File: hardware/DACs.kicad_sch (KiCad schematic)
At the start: 72 parts, among them J20 Conn_01x02, J21 Conn_01x02, U10 LT1678CS8#PBF, U11 LT1678CS8#PBF, U12 LT1678CS8#PBF, U13 LT1678CS8#PBF, U14 LT1461CIS8-2.5#PBF, U6 LTC2642ACDD-16#PBF, U7 LTC2642ACDD-16#PBF, U8 LTC2642ACDD-16#PBF, U9 LTC2642ACDD-16#PBF

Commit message: Some improvements have been made to the layout.
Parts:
- renumbered RShunt1 to RSh1, RShunt2 to RSh2, RShunt3 to RSh3, RShunt4 to RSh4
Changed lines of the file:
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@@
 		(on_board yes)
 		(dnp no)
-		(property "Reference" "RShunt4"
+		(property "Reference" "RSh4"
 			(at 181.102 141.224 0)
 			(effects
@@
 			(project "harp.device.quad.dac"
 				(path "/6b47c519-21c4-43bd-9777-b273999e4447/50574cb8-ffd5-42a3-a56c-0f0945fbd245"
-					(reference "RShunt4")
+					(reference "RSh4")
 					(unit 1)
 				)
@@
 		(on_board yes)
 		(dnp no)
-		(property "Reference" "RShunt2"
+		(property "Reference" "RSh2"
 			(at 181.102 62.484 0)
 			(effects
@@
 			(project "harp.device.quad.dac"
 				(path "/6b47c519-21c4-43bd-9777-b273999e4447/50574cb8-ffd5-42a3-a56c-0f0945fbd245"
-					(reference "RShunt2")
+					(reference "RSh2")
 					(unit 1)
 				)
@@
 		(on_board yes)
 		(dnp no)
-		(property "Reference" "RShunt3"
+		(property "Reference" "RSh3"
 			(at 181.102 101.854 0)
 			(effects
@@
 			(project "harp.device.quad.dac"
 				(path "/6b47c519-21c4-43bd-9777-b273999e4447/50574cb8-ffd5-42a3-a56c-0f0945fbd245"
-					(reference "RShunt3")
+					(reference "RSh3")
 					(unit 1)
 				)
@@
 		(on_board yes)
 		(dnp no)
-		(property "Reference" "RShunt1"
+		(property "Reference" "RSh1"
 			(at 181.102 23.114 0)
 			(effects
@@
 			(project "harp.device.quad.dac"
 				(path "/6b47c519-21c4-43bd-9777-b273999e4447/50574cb8-ffd5-42a3-a56c-0f0945fbd245"
-					(reference "RShunt1")
+					(reference "RSh1")
 					(unit 1)
 				)

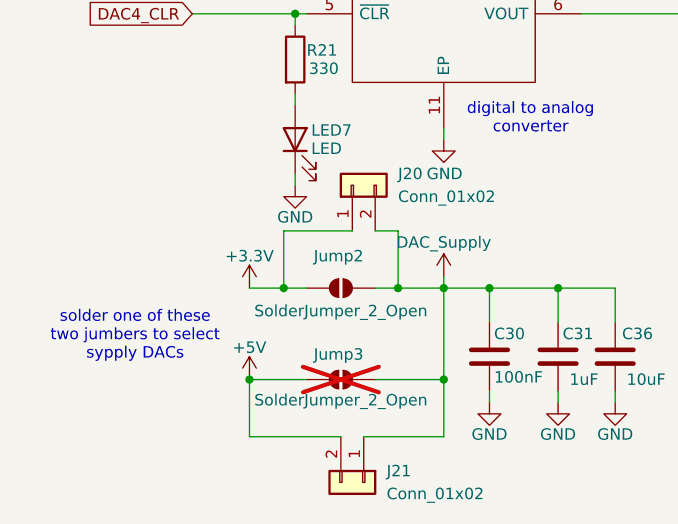
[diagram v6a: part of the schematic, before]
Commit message: Jumpers and interstages connections + added zeners to supply sections + justified text
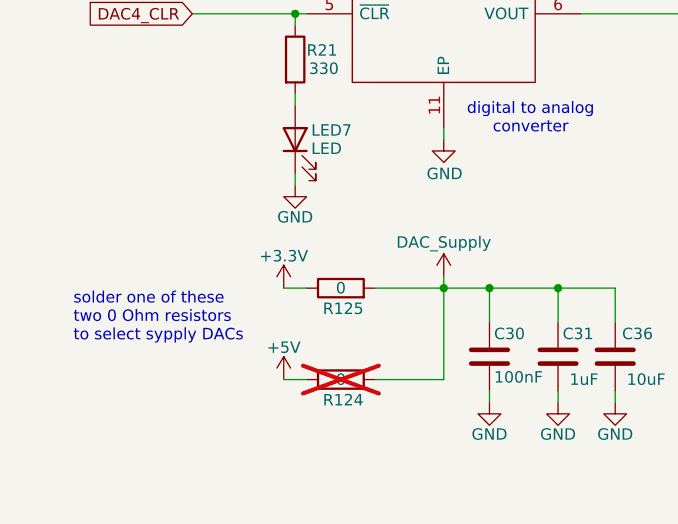
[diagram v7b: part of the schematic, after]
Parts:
- removed J20, J21: Conn_01x02, Connector_PinHeader_2.54mm:PinHeader_1x02_P2.54mm_Vertical, symbol harp.device.quad.dac:Conn_01x02
- removed Jump2, Jump3: SolderJumper_2_Open, harp.device.quad.dac.kicad:R_0603_1608Metric_Pad0.98x0.95mm_HandSolder, symbol harp.device.quad.dac:SolderJumper_2_Open
- added R124, R125: 0, Resistor_SMD:R_0603_1608Metric, symbol harp.device.quad.dac:R_0603
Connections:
- net +3.3V: now also R125.1
- net +5V: now also R124.1
- net DAC_Supply: now also R124.2, R125.2
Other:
- note added: "solder one of these two 0 Ohm resistors to select sypply DACs"
- note removed: "solder one of these two jumbers to select sypply DACs"

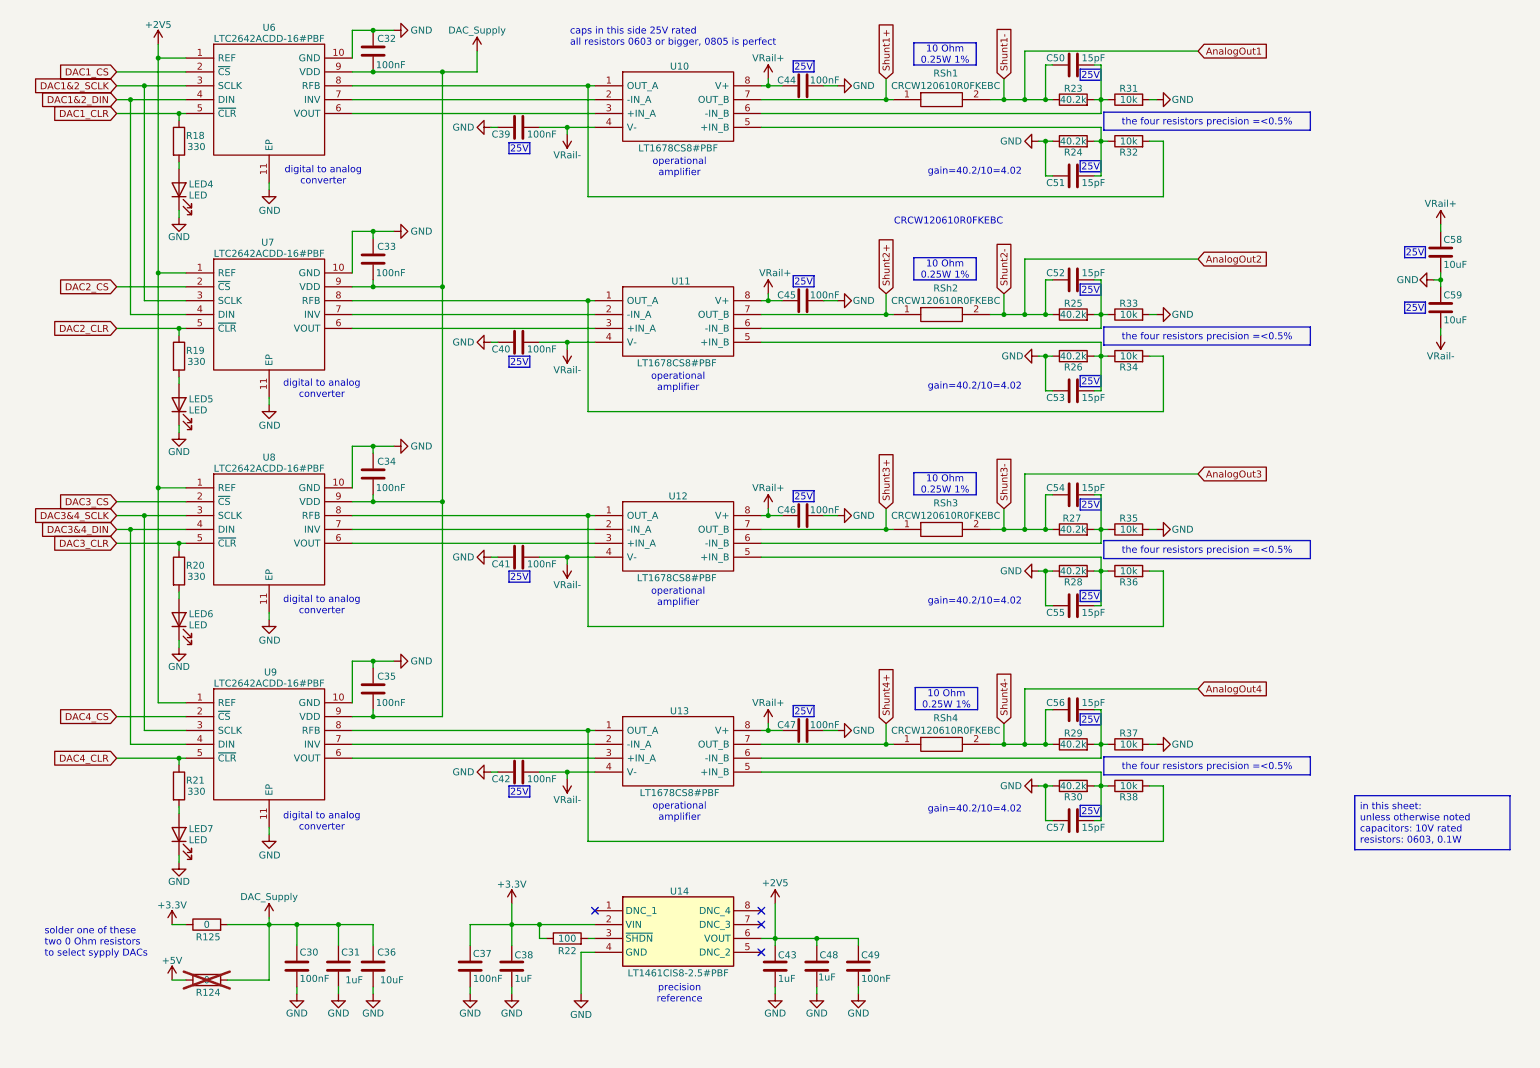
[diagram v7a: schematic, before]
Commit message: The part designators have been reannotated.
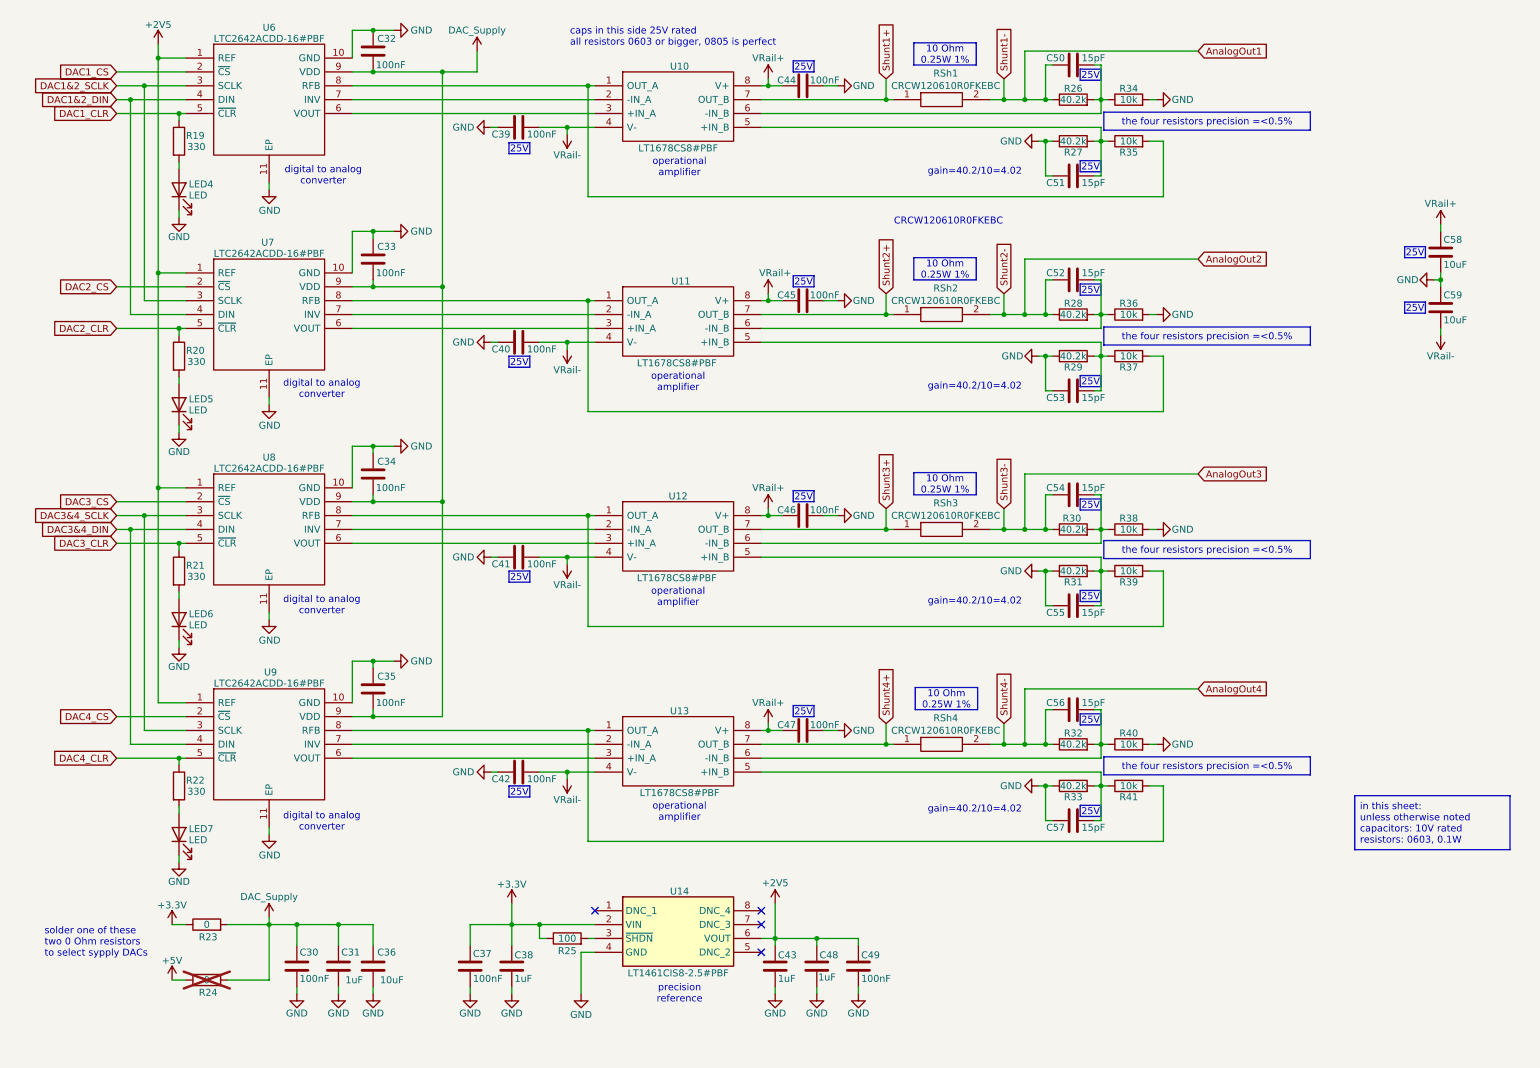
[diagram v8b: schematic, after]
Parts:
- renumbered R18 to R19, R19 to R20, R20 to R21, R21 to R22, R125 to R23, R124 to R24, R22 to R25, R23 to R26, R24 to R27, R25 to R28, R26 to R29, R27 to R30, R28 to R31, R29 to R32, R30 to R33, R31 to R34, R32 to R35, R33 to R36, R34 to R37, R35 to R38, R36 to R39, R37 to R40, R38 to R41
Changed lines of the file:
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@@
 		(on_board yes)
 		(dnp no)
-		(property "Reference" "R25"
+		(property "Reference" "R28"
 			(at 204.47 65.278 90)
 			(effects
@@
 			(project "harp.device.quad.dac"
 				(path "/6b47c519-21c4-43bd-9777-b273999e4447/50574cb8-ffd5-42a3-a56c-0f0945fbd245"
-					(reference "R25")
+					(reference "R28")
 					(unit 1)
 				)
@@
 		(on_board yes)
 		(dnp no)
-		(property "Reference" "R22"
+		(property "Reference" "R25"
 			(at 111.76 183.896 90)
 			(effects
@@
 			(project "harp.device.quad.dac"
 				(path "/6b47c519-21c4-43bd-9777-b273999e4447/50574cb8-ffd5-42a3-a56c-0f0945fbd245"
-					(reference "R22")
+					(reference "R25")
 					(unit 1)
 				)
@@
 		(on_board yes)
 		(dnp no)
-		(property "Reference" "R32"
+		(property "Reference" "R35"
 			(at 214.63 37.592 90)
 			(effects
@@
 			(project "harp.device.quad.dac"
 				(path "/6b47c519-21c4-43bd-9777-b273999e4447/50574cb8-ffd5-42a3-a56c-0f0945fbd245"
-					(reference "R32")
+					(reference "R35")
 					(unit 1)
 				)
@@
 		(on_board yes)
 		(dnp no)
-		(property "Reference" "R23"
+		(property "Reference" "R26"
 			(at 204.47 25.908 90)
 			(effects
@@
 			(project "harp.device.quad.dac"
 				(path "/6b47c519-21c4-43bd-9777-b273999e4447/50574cb8-ffd5-42a3-a56c-0f0945fbd245"
-					(reference "R23")
+					(reference "R26")
 					(unit 1)
 				)
@@
 		(on_board yes)
 		(dnp no)
-		(property "Reference" "R27"
+		(property "Reference" "R30"
 			(at 204.216 104.648 90)
 			(effects
@@
 			(project "harp.device.quad.dac"
 				(path "/6b47c519-21c4-43bd-9777-b273999e4447/50574cb8-ffd5-42a3-a56c-0f0945fbd245"
-					(reference "R27")
+					(reference "R30")
 					(unit 1)
 				)
@@
 		(on_board yes)
 		(dnp no)
-		(property "Reference" "#PWR043"
+		(property "Reference" "#PWR041"
 			(at 36.83 21.59 0)
 			(effects
@@
 			(project "harp.device.quad.dac"
 				(path "/6b47c519-21c4-43bd-9777-b273999e4447/50574cb8-ffd5-42a3-a56c-0f0945fbd245"
-					(reference "#PWR043")
+					(reference "#PWR041")
 					(unit 1)
 				)
@@
 		(on_board yes)
 		(dnp no)
-		(property "Reference" "R36"
+		(property "Reference" "R39"
 			(at 214.63 116.332 90)
 			(effects
@@
 			(project "harp.device.quad.dac"
 				(path "/6b47c519-21c4-43bd-9777-b273999e4447/50574cb8-ffd5-42a3-a56c-0f0945fbd245"
-					(reference "R36")
+					(reference "R39")
 					(unit 1)
 				)
@@
 		(on_board yes)
 		(dnp no)
-		(property "Reference" "R37"
+		(property "Reference" "R40"
 			(at 214.63 144.018 90)
 			(effects
@@
 			(project "harp.device.quad.dac"
 				(path "/6b47c519-21c4-43bd-9777-b273999e4447/50574cb8-ffd5-42a3-a56c-0f0945fbd245"
-					(reference "R37")
+					(reference "R40")
 					(unit 1)
 				)
@@
 		(on_board yes)
 		(dnp no)
-		(property "Reference" "R35"
+		(property "Reference" "R38"
 			(at 214.63 104.648 90)
 			(effects
@@
 			(project "harp.device.quad.dac"
 				(path "/6b47c519-21c4-43bd-9777-b273999e4447/50574cb8-ffd5-42a3-a56c-0f0945fbd245"
-					(reference "R35")
+					(reference "R38")
 					(unit 1)
 				)
@@
 		(on_board yes)
 		(dnp no)
-		(property "Reference" "R30"
+		(property "Reference" "R33"
 			(at 204.47 155.702 90)
 			(effects
@@
 			(project "harp.device.quad.dac"
 				(path "/6b47c519-21c4-43bd-9777-b273999e4447/50574cb8-ffd5-42a3-a56c-0f0945fbd245"
-					(reference "R30")
+					(reference "R33")
 					(unit 1)
 				)
@@
 		(on_board no)
 		(dnp yes)
-		(property "Reference" "R124"
+		(property "Reference" "R24"
 			(at 45.974 191.516 90)
 			(effects
@@
 			(project "harp.device.quad.dac"
 				(path "/6b47c519-21c4-43bd-9777-b273999e4447/50574cb8-ffd5-42a3-a56c-0f0945fbd245"
-					(reference "R124")
+					(reference "R24")
 					(unit 1)
 				)
@@
 		(on_board yes)
 		(dnp no)
-		(property "Reference" "R18"
+		(property "Reference" "R19"
 			(at 41.91 34.544 0)
 			(effects
@@
 			(project "harp.device.quad.dac"
 				(path "/6b47c519-21c4-43bd-9777-b273999e4447/50574cb8-ffd5-42a3-a56c-0f0945fbd245"
-					(reference "R18")
+					(reference "R19")
 					(unit 1)
 				)
@@
 		(on_board yes)
 		(dnp no)
-		(property "Reference" "R125"
+		(property "Reference" "R23"
 			(at 45.974 181.356 90)
 			(effects
@@
 			(project "harp.device.quad.dac"
 				(path "/6b47c519-21c4-43bd-9777-b273999e4447/50574cb8-ffd5-42a3-a56c-0f0945fbd245"
-					(reference "R125")
+					(reference "R23")
 					(unit 1)
 				)
@@
 		(on_board yes)
 		(dnp no)
-		(property "Reference" "R38"
+		(property "Reference" "R41"
 			(at 214.63 155.702 90)
 			(effects
@@
 			(project "harp.device.quad.dac"
 				(path "/6b47c519-21c4-43bd-9777-b273999e4447/50574cb8-ffd5-42a3-a56c-0f0945fbd245"
-					(reference "R38")
+					(reference "R41")
 					(unit 1)
 				)
@@
 		(on_board yes)
 		(dnp no)
-		(property "Reference" "R33"
+		(property "Reference" "R36"
 			(at 214.63 65.278 90)
 			(effects
@@
 			(project "harp.device.quad.dac"
 				(path "/6b47c519-21c4-43bd-9777-b273999e4447/50574cb8-ffd5-42a3-a56c-0f0945fbd245"
-					(reference "R33")
+					(reference "R36")
 					(unit 1)
 				)
@@
 		(on_board yes)
 		(dnp no)
-		(property "Reference" "R31"
+		(property "Reference" "R34"
 			(at 214.63 25.908 90)
 			(effects
@@
 			(project "harp.device.quad.dac"
 				(path "/6b47c519-21c4-43bd-9777-b273999e4447/50574cb8-ffd5-42a3-a56c-0f0945fbd245"
-					(reference "R31")
+					(reference "R34")
 					(unit 1)
 				)
@@
 		(on_board yes)
 		(dnp no)
-		(property "Reference" "R24"
+		(property "Reference" "R27"
 			(at 204.47 37.592 90)
 			(effects
@@
 			(project "harp.device.quad.dac"
 				(path "/6b47c519-21c4-43bd-9777-b273999e4447/50574cb8-ffd5-42a3-a56c-0f0945fbd245"
-					(reference "R24")
+					(reference "R27")
 					(unit 1)
 				)
@@
 		(on_board yes)
 		(dnp no)
-		(property "Reference" "R19"
+		(property "Reference" "R20"
 			(at 41.91 73.914 0)
 			(effects
@@
 			(project "harp.device.quad.dac"
 				(path "/6b47c519-21c4-43bd-9777-b273999e4447/50574cb8-ffd5-42a3-a56c-0f0945fbd245"
-					(reference "R19")
+					(reference "R20")
 					(unit 1)
 				)
@@
 		(on_board yes)
 		(dnp no)
-		(property "Reference" "R34"
+		(property "Reference" "R37"
 			(at 214.63 76.962 90)
 			(effects
@@
 			(project "harp.device.quad.dac"
 				(path "/6b47c519-21c4-43bd-9777-b273999e4447/50574cb8-ffd5-42a3-a56c-0f0945fbd245"
-					(reference "R34")
+					(reference "R37")
 					(unit 1)
 				)
@@
 		(on_board yes)
 		(dnp no)
-		(property "Reference" "R28"
+		(property "Reference" "R31"
 			(at 204.47 116.332 90)
 			(effects
@@
 			(project "harp.device.quad.dac"
 				(path "/6b47c519-21c4-43bd-9777-b273999e4447/50574cb8-ffd5-42a3-a56c-0f0945fbd245"
-					(reference "R28")
+					(reference "R31")
 					(unit 1)
 				)
@@
 		(on_board yes)
 		(dnp no)
-		(property "Reference" "#PWR042"
+		(property "Reference" "#PWR043"
 			(at 39.37 193.04 0)
 			(effects
@@
 			(project "harp.device.quad.dac"
 				(path "/6b47c519-21c4-43bd-9777-b273999e4447/50574cb8-ffd5-42a3-a56c-0f0945fbd245"
-					(reference "#PWR042")
+					(reference "#PWR043")
 					(unit 1)
 				)
@@
 		(on_board yes)
 		(dnp no)
-		(property "Reference" "R20"
+		(property "Reference" "R21"
 			(at 41.91 113.284 0)
 			(effects
@@
 			(project "harp.device.quad.dac"
 				(path "/6b47c519-21c4-43bd-9777-b273999e4447/50574cb8-ffd5-42a3-a56c-0f0945fbd245"
-					(reference "R20")
+					(reference "R21")
 					(unit 1)
 				)
@@
 		(on_board yes)
 		(dnp no)
-		(property "Reference" "#PWR041"
+		(property "Reference" "#PWR042"
 			(at 39.37 182.88 0)
 			(effects
@@
 			(project "harp.device.quad.dac"
 				(path "/6b47c519-21c4-43bd-9777-b273999e4447/50574cb8-ffd5-42a3-a56c-0f0945fbd245"
-					(reference "#PWR041")
+					(reference "#PWR042")
 					(unit 1)
 				)
@@
 		(on_board yes)
 		(dnp no)
-		(property "Reference" "R29"
+		(property "Reference" "R32"
 			(at 204.47 144.018 90)
 			(effects
@@
 			(project "harp.device.quad.dac"
 				(path "/6b47c519-21c4-43bd-9777-b273999e4447/50574cb8-ffd5-42a3-a56c-0f0945fbd245"
-					(reference "R29")
+					(reference "R32")
 					(unit 1)
 				)
@@
 		(on_board yes)
 		(dnp no)
-		(property "Reference" "R26"
+		(property "Reference" "R29"
 			(at 204.47 76.962 90)
 			(effects
@@
 			(project "harp.device.quad.dac"
 				(path "/6b47c519-21c4-43bd-9777-b273999e4447/50574cb8-ffd5-42a3-a56c-0f0945fbd245"
-					(reference "R26")
+					(reference "R29")
 					(unit 1)
 				)
@@
 		(on_board yes)
 		(dnp no)
-		(property "Reference" "R21"
+		(property "Reference" "R22"
 			(at 41.91 152.654 0)
 			(effects
@@
 			(project "harp.device.quad.dac"
 				(path "/6b47c519-21c4-43bd-9777-b273999e4447/50574cb8-ffd5-42a3-a56c-0f0945fbd245"
-					(reference "R21")
+					(reference "R22")
 					(unit 1)
 				)
